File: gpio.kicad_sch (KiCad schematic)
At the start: 15 parts, among them Q3 AUIRF7316QTR, Q4 AUIRF7316QTR, Q5 AUIRF7316QTR, Q6 AUIRF7316QTR, U7 NPIC6C596ADJ, U8 PCF8574DWR

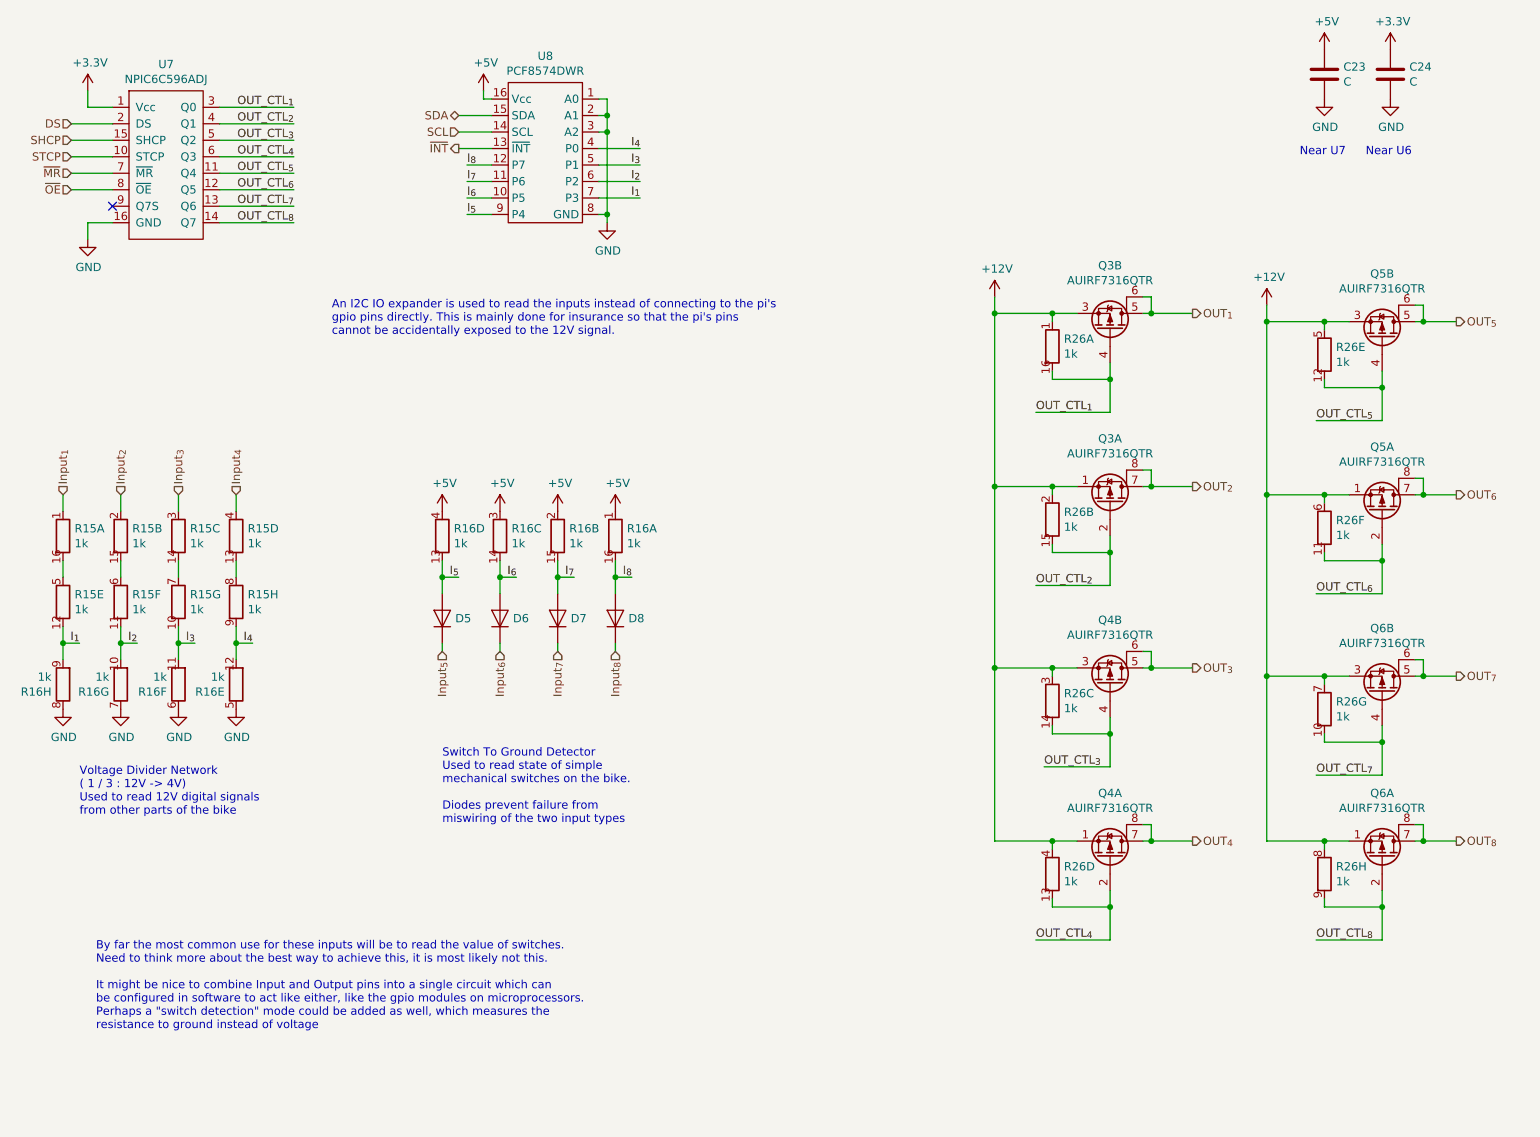
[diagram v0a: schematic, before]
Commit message: Cleaning up
Reassigned reference designators to better match their position on the board.
Moved USB hub IC and related circuits to their own sheet in the schematic.
Tweaked reference designator positions on board to improve visibility.
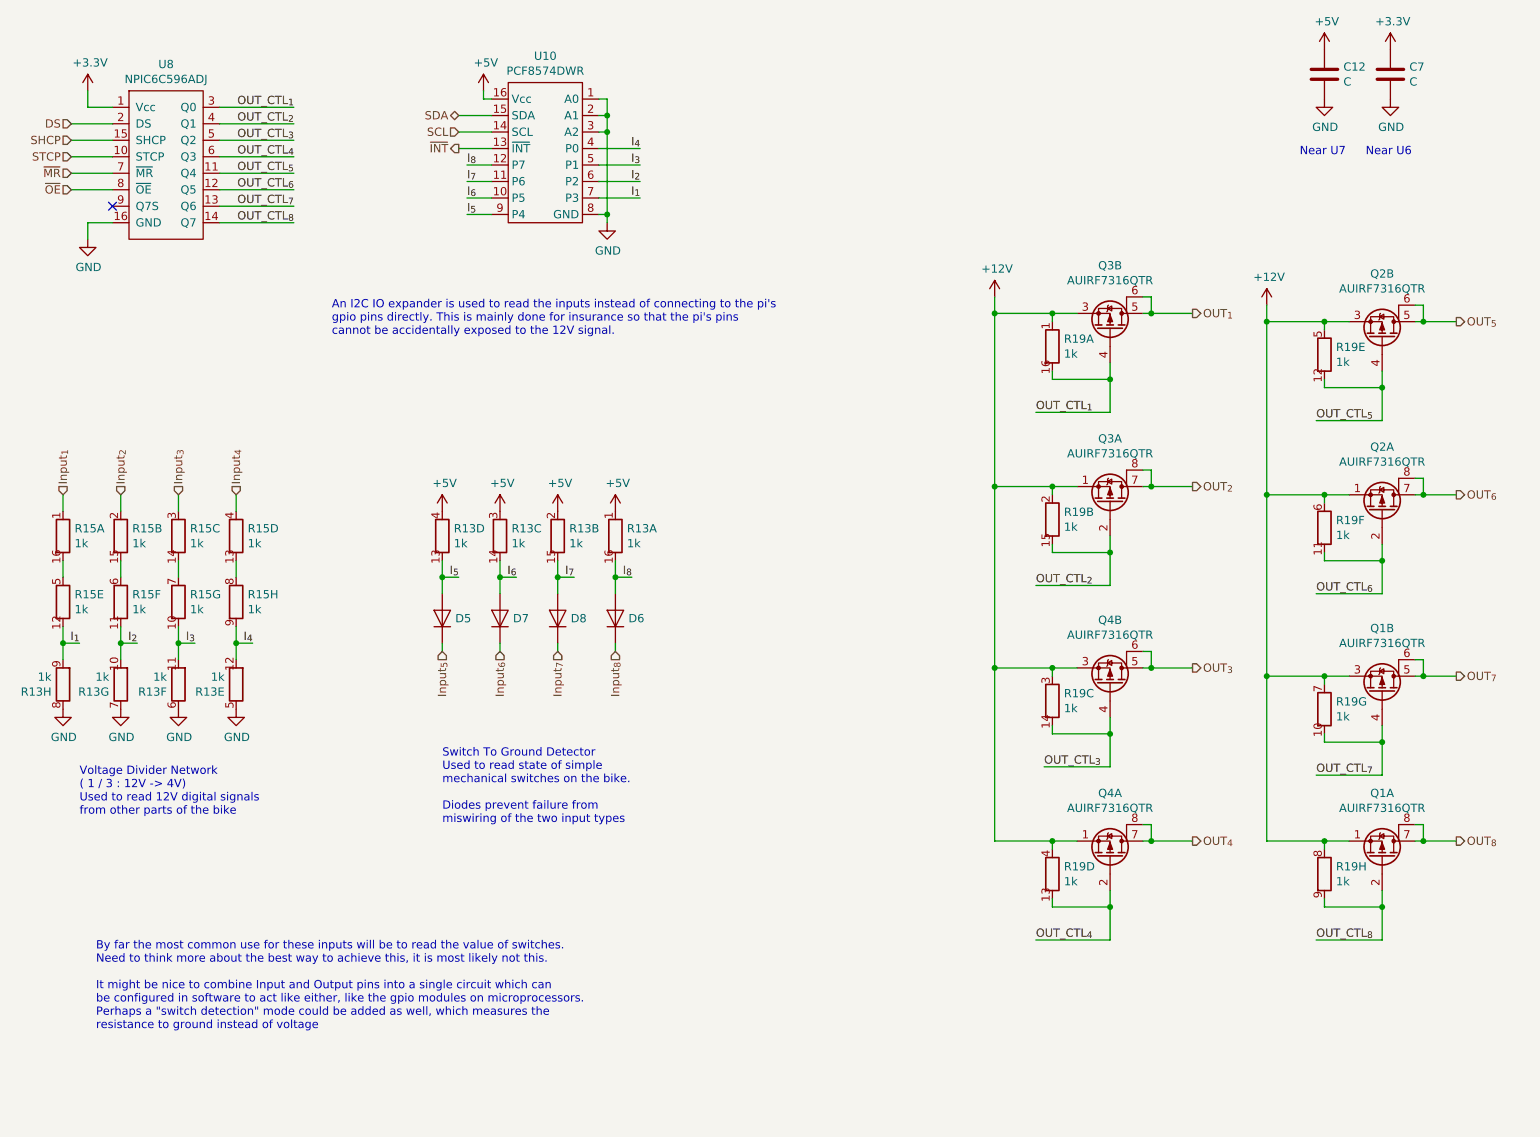
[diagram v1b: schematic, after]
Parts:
- renumbered C23 to C12, C24 to C7, D8 to D6, D6 to D7, D7 to D8, Q6 to Q1, Q5 to Q2, R16 to R13, R26 to R19, U8 to U10, U7 to U8
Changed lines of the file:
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@@
   (title_block
     (title "Dennis")
-    (date "2021-02-26")
-    (rev "0.1.2")
+    (date "2021-03-30")
+    (rev "0.1.3")
     (company "eCafe Racer")
   )
@@
   (symbol (lib_name "symbols:CTS-766161102GP_4") (lib_id "symbols:CTS-766161102GP") (at 31.75 125.73 180) (unit 8)
     (in_bom yes) (on_board yes)
-    (property "Reference" "R16" (id 0) (at 29.972 126.879 0)
+    (property "Reference" "R13" (id 0) (at 29.972 126.879 0)
       (effects (font (size 1.27 1.27)) (justify left))
     )
@@
   (symbol (lib_name "symbols:CTS-766161102GP_1") (lib_id "symbols:CTS-766161102GP") (at 40.64 125.73 180) (unit 7)
     (in_bom yes) (on_board yes)
-    (property "Reference" "R16" (id 0) (at 38.862 126.879 0)
+    (property "Reference" "R13" (id 0) (at 38.862 126.879 0)
       (effects (font (size 1.27 1.27)) (justify left))
     )
@@
   (symbol (lib_name "symbols:CTS-766161102GP_3") (lib_id "symbols:CTS-766161102GP") (at 49.53 125.73 180) (unit 6)
     (in_bom yes) (on_board yes)
-    (property "Reference" "R16" (id 0) (at 47.752 126.879 0)
+    (property "Reference" "R13" (id 0) (at 47.752 126.879 0)
       (effects (font (size 1.27 1.27)) (justify left))
     )
@@
   (symbol (lib_name "symbols:CTS-766161102GP_2") (lib_id "symbols:CTS-766161102GP") (at 58.42 125.73 180) (unit 5)
     (in_bom yes) (on_board yes)
-    (property "Reference" "R16" (id 0) (at 56.642 126.879 0)
+    (property "Reference" "R13" (id 0) (at 56.642 126.879 0)
       (effects (font (size 1.27 1.27)) (justify left))
     )
@@
   (symbol (lib_name "symbols:CTS-766161102GP_5") (lib_id "symbols:CTS-766161102GP") (at 90.17 102.87 0) (unit 4)
     (in_bom yes) (on_board yes)
-    (property "Reference" "R16" (id 0) (at 91.948 101.721 0)
+    (property "Reference" "R13" (id 0) (at 91.948 101.721 0)
       (effects (font (size 1.27 1.27)) (justify left))
     )
@@
   (symbol (lib_name "symbols:CTS-766161102GP_6") (lib_id "symbols:CTS-766161102GP") (at 99.06 102.87 0) (unit 3)
     (in_bom yes) (on_board yes)
-    (property "Reference" "R16" (id 0) (at 100.838 101.721 0)
+    (property "Reference" "R13" (id 0) (at 100.838 101.721 0)
       (effects (font (size 1.27 1.27)) (justify left))
     )
@@
   (symbol (lib_name "symbols:CTS-766161102GP_7") (lib_id "symbols:CTS-766161102GP") (at 107.95 102.87 0) (unit 2)
     (in_bom yes) (on_board yes)
-    (property "Reference" "R16" (id 0) (at 109.728 101.721 0)
+    (property "Reference" "R13" (id 0) (at 109.728 101.721 0)
       (effects (font (size 1.27 1.27)) (justify left))
     )
@@
   (symbol (lib_name "symbols:CTS-766161102GP_8") (lib_id "symbols:CTS-766161102GP") (at 116.84 102.87 0) (unit 1)
     (in_bom yes) (on_board yes)
-    (property "Reference" "R16" (id 0) (at 118.618 101.721 0)
+    (property "Reference" "R13" (id 0) (at 118.618 101.721 0)
       (effects (font (size 1.27 1.27)) (justify left))
     )
@@
   (symbol (lib_name "symbols:CTS-766161102GP_18") (lib_id "symbols:CTS-766161102GP") (at 184.15 73.66 0) (unit 1)
     (in_bom yes) (on_board yes)
-    (property "Reference" "R26" (id 0) (at 185.9281 72.5106 0)
+    (property "Reference" "R19" (id 0) (at 185.9281 72.5106 0)
       (effects (font (size 1.27 1.27)) (justify left))
     )
@@
   (symbol (lib_name "symbols:CTS-766161102GP_17") (lib_id "symbols:CTS-766161102GP") (at 184.15 100.33 0) (unit 2)
     (in_bom yes) (on_board yes)
-    (property "Reference" "R26" (id 0) (at 185.9281 99.1806 0)
+    (property "Reference" "R19" (id 0) (at 185.9281 99.1806 0)
       (effects (font (size 1.27 1.27)) (justify left))
     )
@@
   (symbol (lib_name "symbols:CTS-766161102GP_23") (lib_id "symbols:CTS-766161102GP") (at 184.15 128.27 0) (unit 3)
     (in_bom yes) (on_board yes)
-    (property "Reference" "R26" (id 0) (at 185.9281 127.1206 0)
+    (property "Reference" "R19" (id 0) (at 185.9281 127.1206 0)
       (effects (font (size 1.27 1.27)) (justify left))
     )
@@
   (symbol (lib_id "symbols:CTS-766161102GP") (at 184.15 154.94 0) (unit 4)
     (in_bom yes) (on_board yes)
-    (property "Reference" "R26" (id 0) (at 185.9281 153.7906 0)
+    (property "Reference" "R19" (id 0) (at 185.9281 153.7906 0)
       (effects (font (size 1.27 1.27)) (justify left))
     )
@@
   (symbol (lib_name "symbols:CTS-766161102GP_22") (lib_id "symbols:CTS-766161102GP") (at 226.06 74.93 0) (unit 5)
     (in_bom yes) (on_board yes)
-    (property "Reference" "R26" (id 0) (at 227.8381 73.7806 0)
+    (property "Reference" "R19" (id 0) (at 227.8381 73.7806 0)
       (effects (font (size 1.27 1.27)) (justify left))
     )
@@
   (symbol (lib_name "symbols:CTS-766161102GP_19") (lib_id "symbols:CTS-766161102GP") (at 226.06 101.6 0) (unit 6)
     (in_bom yes) (on_board yes)
-    (property "Reference" "R26" (id 0) (at 227.8381 100.4506 0)
+    (property "Reference" "R19" (id 0) (at 227.8381 100.4506 0)
       (effects (font (size 1.27 1.27)) (justify left))
     )
@@
   (symbol (lib_name "symbols:CTS-766161102GP_20") (lib_id "symbols:CTS-766161102GP") (at 226.06 129.54 0) (unit 7)
     (in_bom yes) (on_board yes)
-    (property "Reference" "R26" (id 0) (at 227.8381 128.3906 0)
+    (property "Reference" "R19" (id 0) (at 227.8381 128.3906 0)
       (effects (font (size 1.27 1.27)) (justify left))
     )
@@
   (symbol (lib_name "symbols:CTS-766161102GP_21") (lib_id "symbols:CTS-766161102GP") (at 226.06 154.94 0) (unit 8)
     (in_bom yes) (on_board yes)
-    (property "Reference" "R26" (id 0) (at 227.8381 153.7906 0)
+    (property "Reference" "R19" (id 0) (at 227.8381 153.7906 0)
       (effects (font (size 1.27 1.27)) (justify left))
     )
@@
   (symbol (lib_id "symbols:Diode") (at 99.06 115.57 90) (unit 1)
     (in_bom yes) (on_board yes)
-    (property "Reference" "D6" (id 0) (at 101.067 115.57 90)
+    (property "Reference" "D7" (id 0) (at 101.067 115.57 90)
       (effects (font (size 1.27 1.27)) (justify right))
     )
@@
   (symbol (lib_id "symbols:Diode") (at 107.95 115.57 90) (unit 1)
     (in_bom yes) (on_board yes)
-    (property "Reference" "D7" (id 0) (at 109.957 115.57 90)
+    (property "Reference" "D8" (id 0) (at 109.957 115.57 90)
       (effects (font (size 1.27 1.27)) (justify right))
     )
@@
   (symbol (lib_id "symbols:Diode") (at 116.84 115.57 90) (unit 1)
     (in_bom yes) (on_board yes)
-    (property "Reference" "D8" (id 0) (at 118.847 115.57 90)
+    (property "Reference" "D6" (id 0) (at 118.847 115.57 90)
       (effects (font (size 1.27 1.27)) (justify right))
     )
@@
   (symbol (lib_id "Device:C") (at 226.06 31.75 0) (unit 1)
     (in_bom yes) (on_board yes)
-    (property "Reference" "C23" (id 0) (at 228.9811 30.6006 0)
+    (property "Reference" "C12" (id 0) (at 228.9811 30.6006 0)
       (effects (font (size 1.27 1.27)) (justify left))
     )
@@
   (symbol (lib_id "Device:C") (at 236.22 31.75 0) (unit 1)
     (in_bom yes) (on_board yes)
-    (property "Reference" "C24" (id 0) (at 239.1411 30.6006 0)
+    (property "Reference" "C7" (id 0) (at 239.1411 30.6006 0)
       (effects (font (size 1.27 1.27)) (justify left))
     )
@@
   (symbol (lib_name "symbols:AUIRF7316QTR_6") (lib_id "symbols:AUIRF7316QTR") (at 234.95 71.12 270) (mirror x) (unit 2)
     (in_bom yes) (on_board yes)
-    (property "Reference" "Q5" (id 0) (at 234.95 62.4775 90))
+    (property "Reference" "Q2" (id 0) (at 234.95 62.4775 90))
     (property "Value" "AUIRF7316QTR" (id 1) (at 234.95 64.7762 90))
     (property "Footprint" "Package_SO:SO-8_3.9x4.9mm_P1.27mm" (id 2) (at 253.5428 72.4916 0)
@@
   (symbol (lib_name "symbols:AUIRF7316QTR_7") (lib_id "symbols:AUIRF7316QTR") (at 234.95 97.79 270) (mirror x) (unit 1)
     (in_bom yes) (on_board yes)
-    (property "Reference" "Q5" (id 0) (at 234.95 89.1475 90))
+    (property "Reference" "Q2" (id 0) (at 234.95 89.1475 90))
     (property "Value" "AUIRF7316QTR" (id 1) (at 234.95 91.4462 90))
     (property "Footprint" "Package_SO:SO-8_3.9x4.9mm_P1.27mm" (id 2) (at 253.5428 99.1616 0)
@@
   (symbol (lib_name "symbols:AUIRF7316QTR_8") (lib_id "symbols:AUIRF7316QTR") (at 234.95 125.73 270) (mirror x) (unit 2)
     (in_bom yes) (on_board yes)
-    (property "Reference" "Q6" (id 0) (at 234.95 117.0875 90))
+    (property "Reference" "Q1" (id 0) (at 234.95 117.0875 90))
     (property "Value" "AUIRF7316QTR" (id 1) (at 234.95 119.3862 90))
     (property "Footprint" "Package_SO:SO-8_3.9x4.9mm_P1.27mm" (id 2) (at 253.5428 127.1016 0)
@@
   (symbol (lib_name "symbols:AUIRF7316QTR_1") (lib_id "symbols:AUIRF7316QTR") (at 234.95 151.13 270) (mirror x) (unit 1)
     (in_bom yes) (on_board yes)
-    (property "Reference" "Q6" (id 0) (at 234.95 142.4875 90))
+    (property "Reference" "Q1" (id 0) (at 234.95 142.4875 90))
     (property "Value" "AUIRF7316QTR" (id 1) (at 234.95 144.7862 90))
     (property "Footprint" "Package_SO:SO-8_3.9x4.9mm_P1.27mm" (id 2) (at 253.5428 152.5016 0)
@@
   (symbol (lib_id "symbols:PCF8574DWR") (at 106.68 44.45 0) (mirror y) (unit 1)
     (in_bom yes) (on_board yes)
-    (property "Reference" "U8" (id 0) (at 106.045 28.9365 0))
+    (property "Reference" "U10" (id 0) (at 106.045 28.9365 0))
     (property "Value" "PCF8574DWR" (id 1) (at 106.045 31.2352 0))
     (property "Footprint" "Package_SO:SOIC-16W_7.5x10.3mm_P1.27mm" (id 2) (at 110.49 30.48 0)
@@
   (symbol (lib_id "Custom-Symbols:NPIC6C596ADJ") (at 48.26 45.72 0) (unit 1)
     (in_bom yes) (on_board yes)
-    (property "Reference" "U7" (id 0) (at 47.625 30.2068 0))
+    (property "Reference" "U8" (id 0) (at 47.625 30.2068 0))
     (property "Value" "NPIC6C596ADJ" (id 1) (at 47.625 32.5055 0))
     (property "Footprint" "Package_SO:SOIC-16_4.55x10.3mm_P1.27mm" (id 2) (at 58.42 31.75 0)

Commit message: migrated computers
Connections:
- net ~INT renamed ~{INT}
- net ~MR renamed ~{MR}
- net ~OE renamed ~{OE}

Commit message: layout sketching
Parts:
- removed D5, D7: Diode, Diode_SMD:D_SOD-123F, symbol symbols:Diode
- removed R13, R15: CTS-766161102GP, Package_SO:SOIC-16_3.9x9.9mm_P1.27mm, symbol symbols:CTS-766161102GP
- added D11: LED_Green, LED_SMD:LED_0805_2012Metric_Pad1.15x1.40mm_HandSolder, symbol ecafe-racer:LED_Green
- added R11, R12, R13, R14, R15, R16, R9: R, Resistor_SMD:R_0805_2012Metric, symbol Device:R
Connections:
- net Input_{7} is gone; now on net Input_{4}: D8.1 (K)
- net Input_{8} is gone; now on net Input_{3}: D6.1 (K)
- net +5V: now also R14.1, R15.1
- net GND: now also D11.1, R11.2, R13.2
- net Input_{1}: now also R9.1
- net Input_{2}: now also R12.1
- net OUT_CTL_{8}: no longer U8.14 (Q7)
- net I_{5}: no longer names the net of U10.9 (P4)
- net I_{6}: no longer names the net of U10.10 (P5)
- net I_{7}: no longer names the net of U10.11 (P6)
- net I_{7}: no longer D8.2 (A)
- net I_{8}: no longer names the net of U10.12 (P7)
- net I_{8}: no longer D6.2 (A)
- new net: D11.2, R16.2
- new net In_{1}: R11.1, R9.2
- new net In_{2}: R12.2, R13.1
- new net In_{3}: D8.2 (A), R14.2
- new net In_{4}: D6.2 (A), R15.2
- new net SHIFT_IND: R16.1, U8.14 (Q7)
- no-connect marks 1 -> 5
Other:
- moved on the sheet: D6, D8
